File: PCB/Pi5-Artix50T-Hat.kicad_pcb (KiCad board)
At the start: 4 copper layers, 65 x 56 mm, 159 parts, among them J1 GPIO, J2 Molex 0878321420, J3 68711614522, J4 Molex 0878321420, U1 BL24C256A, U10 AP62200TWU-7, U11 AP62200TWU-7, U12 AP62200TWU-7, U2 XC7A50T-FGG484, U9 AP62200TWU-7, X1 50MHz

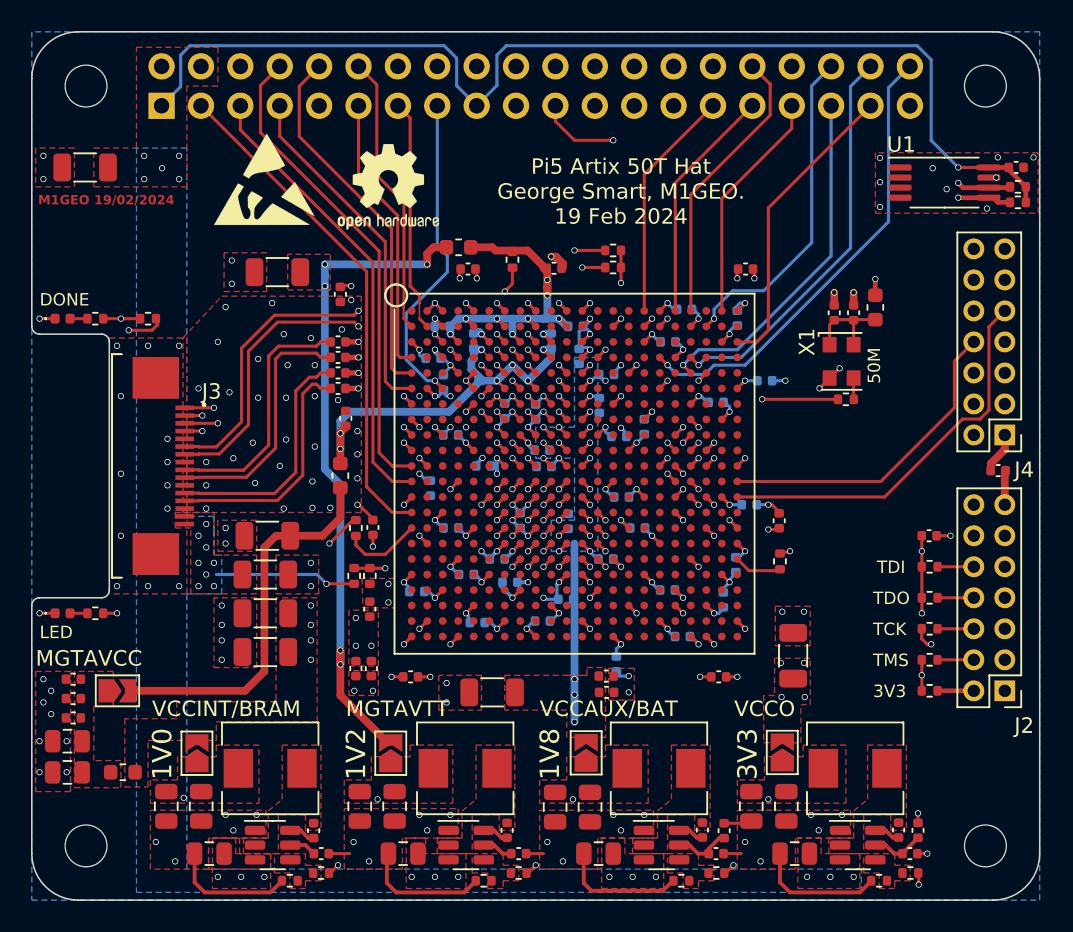
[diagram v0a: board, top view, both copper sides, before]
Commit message: Updated PCB to remove MOSI-MISO cross. Updated texts. New images.
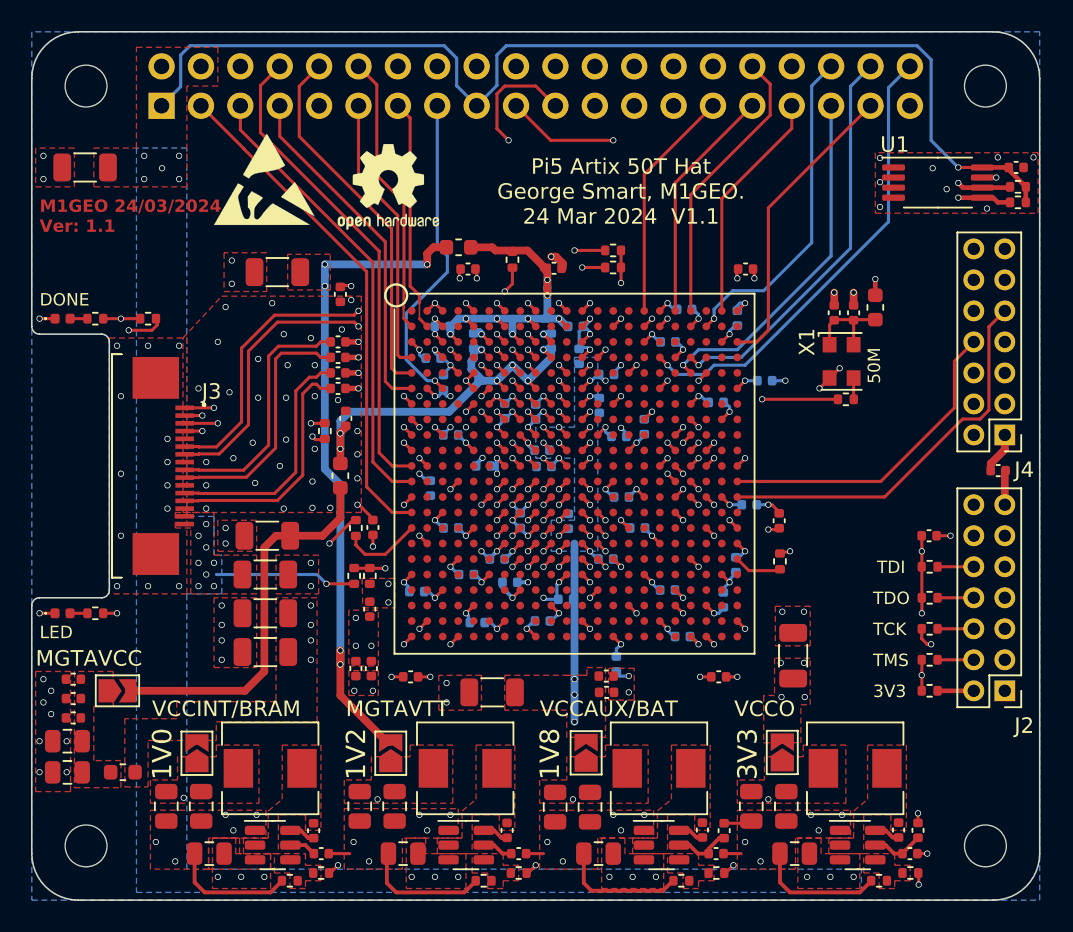
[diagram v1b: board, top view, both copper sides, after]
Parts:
- added R19: 3.2k, Resistor_SMD:R_0402_1005Metric, F.Cu at (118.9, 69.8)
- moved U1 0.43 mm to (158.4, 53.7)
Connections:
- U2 pad AB20: /Raspberry Pi 5/GPIO10/SPI0.MOSI -> /Raspberry Pi 5/GPIO9/SPI0.MISO
- U2 pad K1: /FPGA Top/PCIE_DET_WAKE -> Net-(U2C-IO_L7P_T1_AD6P_35)
- U2 pad R22: /Raspberry Pi 5/GPIO9/SPI0.MISO -> /Raspberry Pi 5/GPIO10/SPI0.MOSI
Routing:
- net /Raspberry Pi 5/GPIO9/SPI0.MISO: track 37.9 -> 52.0 mm
- net Net-(U2C-IO_L7P_T1_AD6P_35): track 0.00 -> 8.48 mm, vias 0 -> 2
- net /Raspberry Pi 5/GPIO10/SPI0.MOSI: track 46.3 -> 39.9 mm, vias 1 -> 2
- net /FPGA Top/PCIE_DET_WAKE: track 15.4 -> 9.14 mm
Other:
- board text added: "24 Mar 2024 - V1.1 - Pi5 Artix 50T Hat"
- board text added: "M1GEO 24/03/2024 Ver: 1.1"
- board text added: "Pi5 Artix 50T Hat George Smart, M1GEO. 24 Mar 2024 V1.1"
- board text removed: "19 Feb 2024 - Pi5 Artix 50T Hat"
- board text removed: "JLCJLCJLC"
- board text removed: "M1GEO 19/02/2024"
- board text removed: "Pi5 Artix 50T Hat George Smart, M1GEO. 19 Feb 2024"
